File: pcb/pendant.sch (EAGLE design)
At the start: 73 parts, among them CON1 USB_MICROSMT+THRUHULE, Q2 16MHz, SW2 BUTTON_2, T1 SSM3J328R,LF, T2 SSM3J328R,LF, U2 MK20D--VFM5, U3 74LVC1G17DCK, U4 74LVC1G17DCK

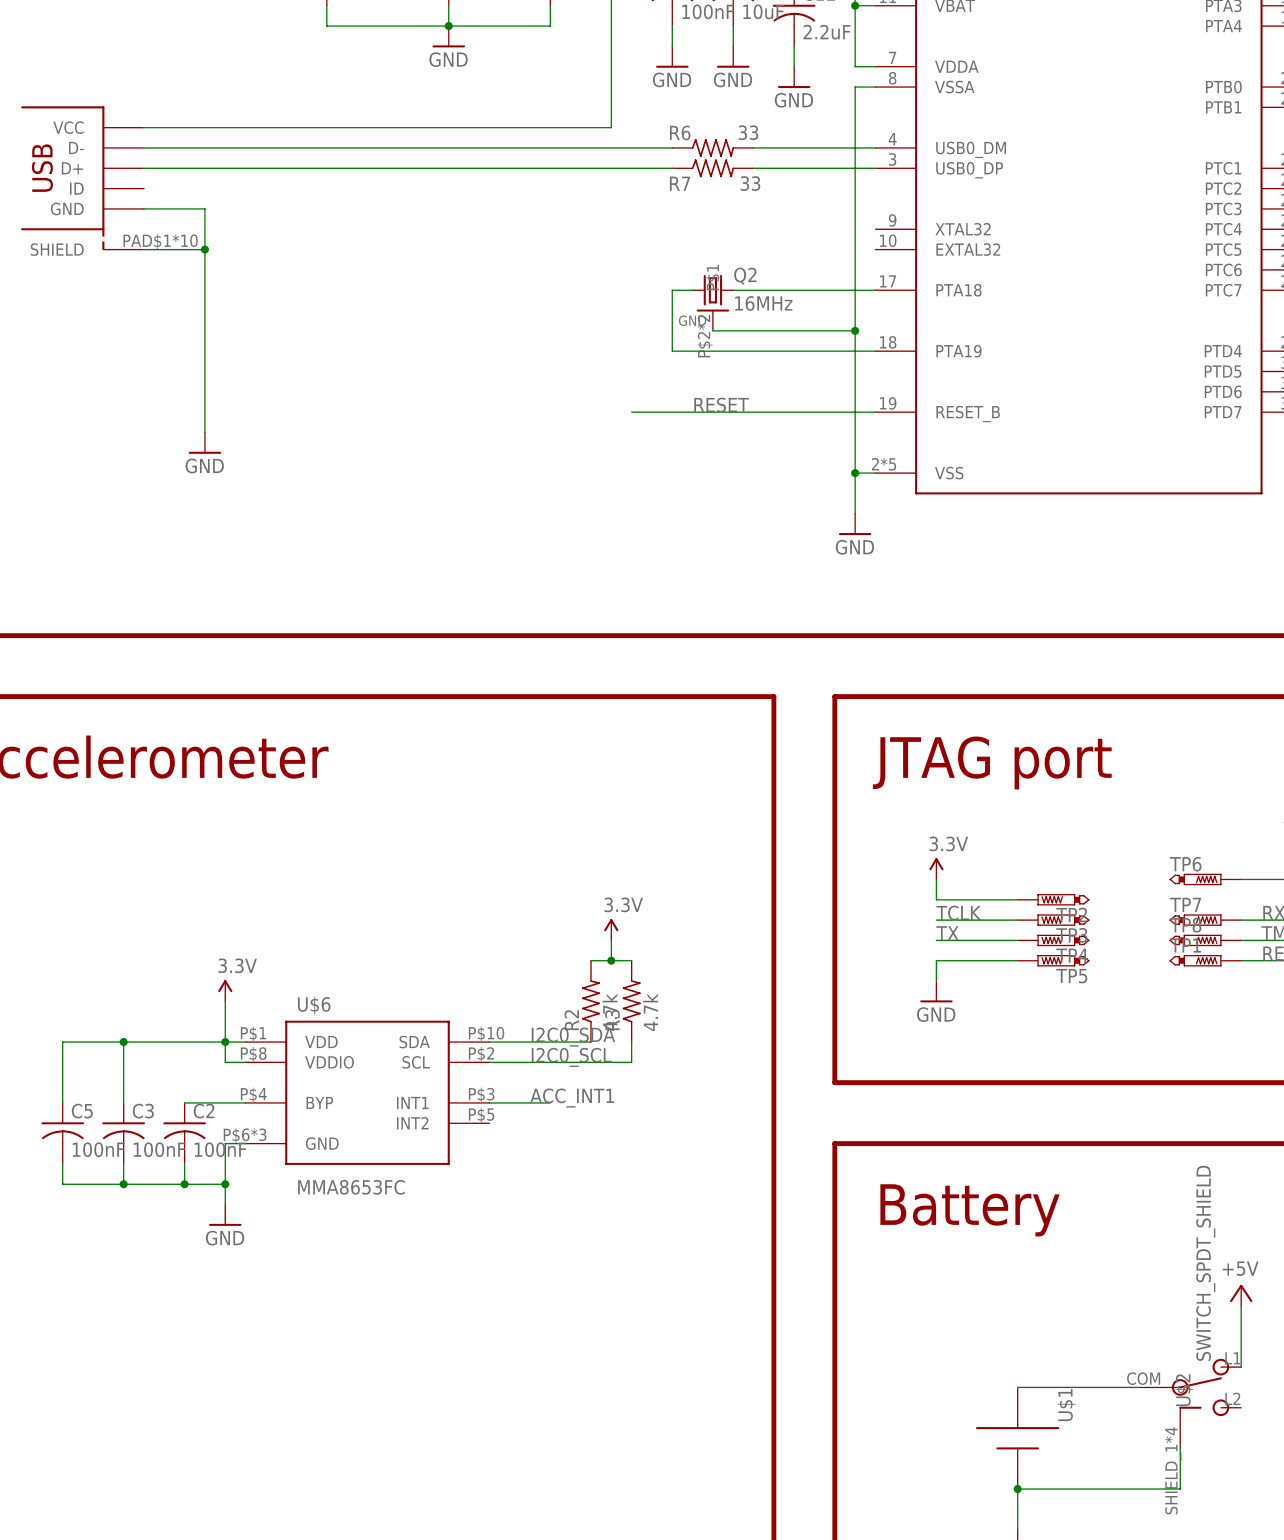
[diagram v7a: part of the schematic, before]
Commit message: Add USB, VBAT test points
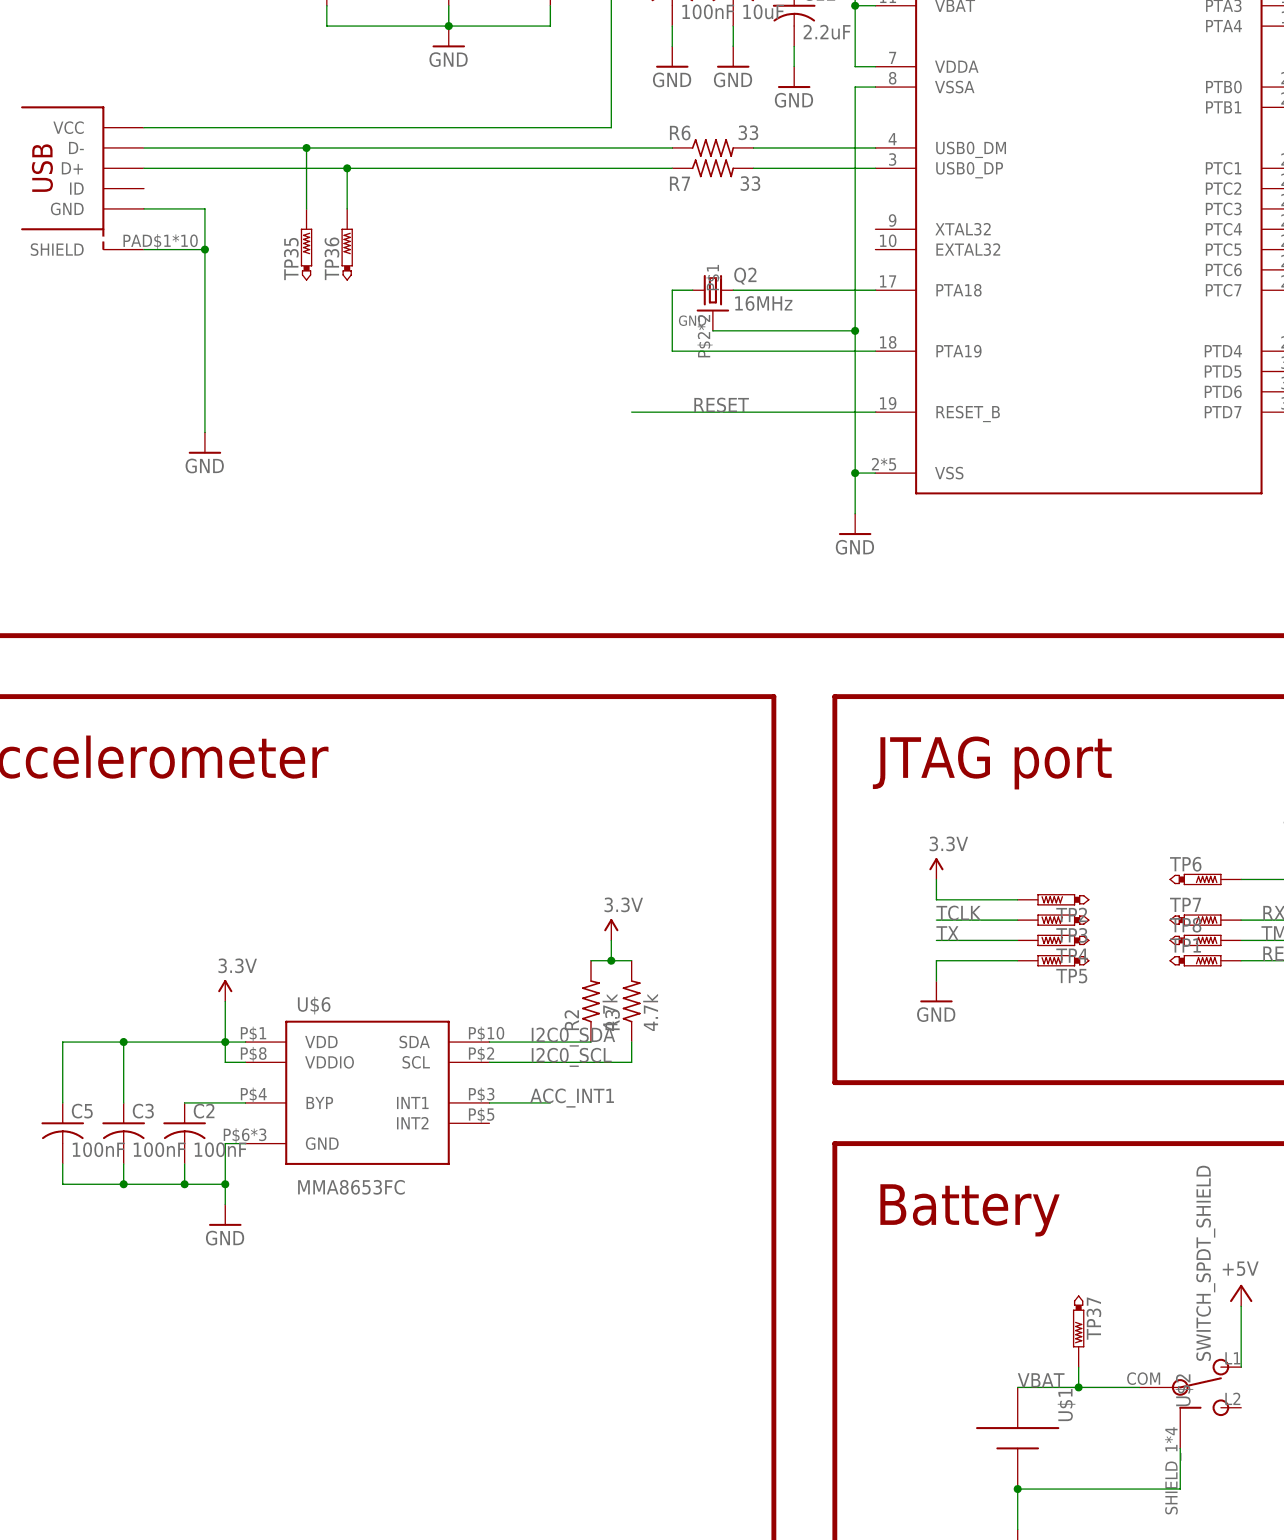
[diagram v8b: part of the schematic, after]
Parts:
- added TP35, TP36, TP37: PTR1B1,27, testpad:PTR1B1,27
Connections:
- removed net N$2: U$1.+, U$2.COM
- new net VBAT: TP37.TP, U$1.+, U$2.COM
- net N$14: now also TP36.TP
- net N$21: now also TP35.TP
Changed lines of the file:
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@@
 <part name="TP33" library="testpad" deviceset="PTR1" device="B1,27"/>
 <part name="TP34" library="testpad" deviceset="PTR1" device="B1,27"/>
+<part name="TP35" library="testpad" deviceset="PTR1" device="B1,27"/>
+<part name="TP36" library="testpad" deviceset="PTR1" device="B1,27"/>
+<part name="TP37" library="testpad" deviceset="PTR1" device="B1,27"/>
 </parts>
 <sheets>
@@
 <instance part="TP33" gate="G$1" x="393.7" y="251.46" rot="R90"/>
 <instance part="TP34" gate="G$1" x="393.7" y="226.06" rot="R90"/>
+<instance part="TP35" gate="G$1" x="73.66" y="309.88"/>
+<instance part="TP36" gate="G$1" x="78.74" y="309.88"/>
+<instance part="TP37" gate="G$1" x="170.18" y="170.18" rot="R180"/>
 </instances>
 <busses>
@@
 <pinref part="R7" gate="G$1" pin="1"/>
 <pinref part="CON1" gate="G$1" pin="D+"/>
-<wire x1="119.38" y1="317.5" x2="53.34" y2="317.5" width="0.1524" layer="91"/>
+<wire x1="119.38" y1="317.5" x2="78.74" y2="317.5" width="0.1524" layer="91"/>
+<pinref part="TP36" gate="G$1" pin="TP"/>
+<wire x1="78.74" y1="317.5" x2="53.34" y2="317.5" width="0.1524" layer="91"/>
+<wire x1="78.74" y1="317.5" x2="78.74" y2="312.42" width="0.1524" layer="91"/>
+<junction x="78.74" y="317.5"/>
 </segment>
 </net>
@@
 <pinref part="R6" gate="G$1" pin="1"/>
 <pinref part="CON1" gate="G$1" pin="D-"/>
-<wire x1="53.34" y1="320.04" x2="119.38" y2="320.04" width="0.1524" layer="91"/>
+<wire x1="53.34" y1="320.04" x2="73.66" y2="320.04" width="0.1524" layer="91"/>
+<pinref part="TP35" gate="G$1" pin="TP"/>
+<wire x1="73.66" y1="320.04" x2="119.38" y2="320.04" width="0.1524" layer="91"/>
+<wire x1="73.66" y1="312.42" x2="73.66" y2="320.04" width="0.1524" layer="91"/>
+<junction x="73.66" y="320.04"/>
 </segment>
 </net>
@@
 </segment>
 </net>
-<net name="N$2" class="0">
+<net name="VBAT" class="0">
 <segment>
 <pinref part="U$1" gate="G$1" pin="+"/>
-<wire x1="162.56" y1="165.1" x2="177.8" y2="165.1" width="0.1524" layer="91"/>
+<wire x1="162.56" y1="165.1" x2="170.18" y2="165.1" width="0.1524" layer="91"/>
 <pinref part="U$2" gate="G$1" pin="COM"/>
-</segment>
-</net>
+<pinref part="TP37" gate="G$1" pin="TP"/>
+<wire x1="170.18" y1="165.1" x2="177.8" y2="165.1" width="0.1524" layer="91"/>
+<wire x1="170.18" y1="167.64" x2="170.18" y2="165.1" width="0.1524" layer="91"/>
+<junction x="170.18" y="165.1"/>
+<label x="162.56" y="165.1" size="1.778" layer="95"/>
+</segment>
+</net>
